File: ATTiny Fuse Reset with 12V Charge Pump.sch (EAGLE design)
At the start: 37 parts, among them IC1 ATTinyx5/13, IC2 ATTinyx4, U2 ARDUINOR3-BPLACE

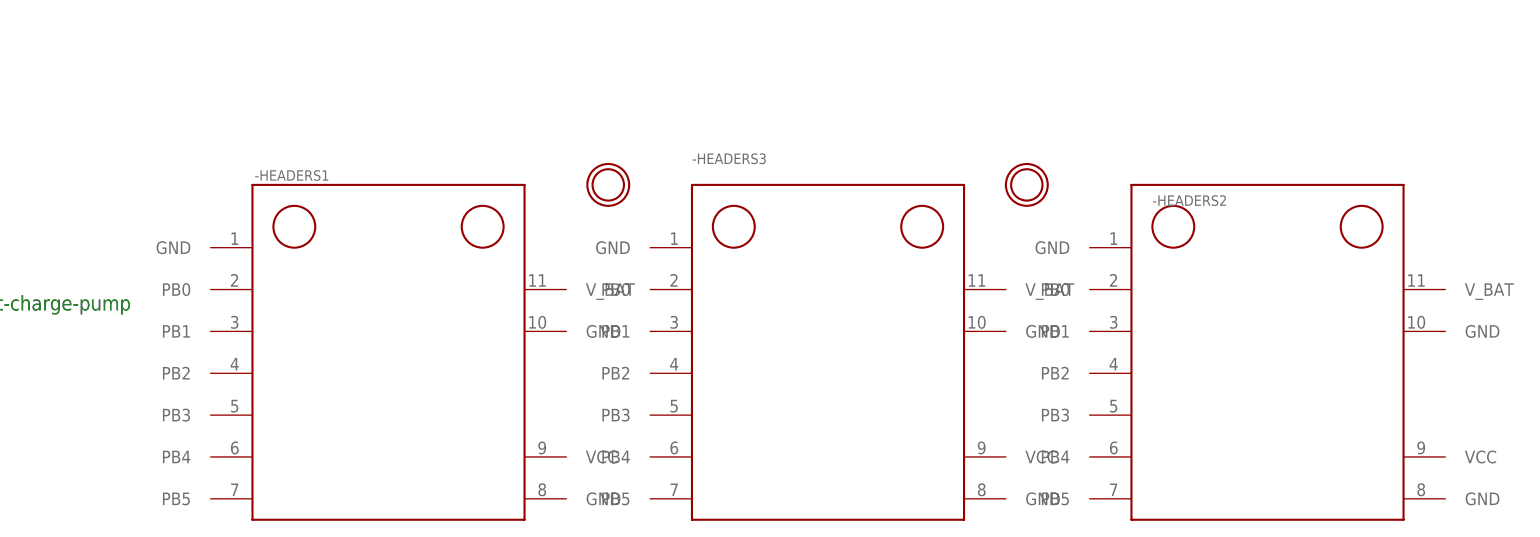
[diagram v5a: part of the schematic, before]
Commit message: changed attiny breakout size
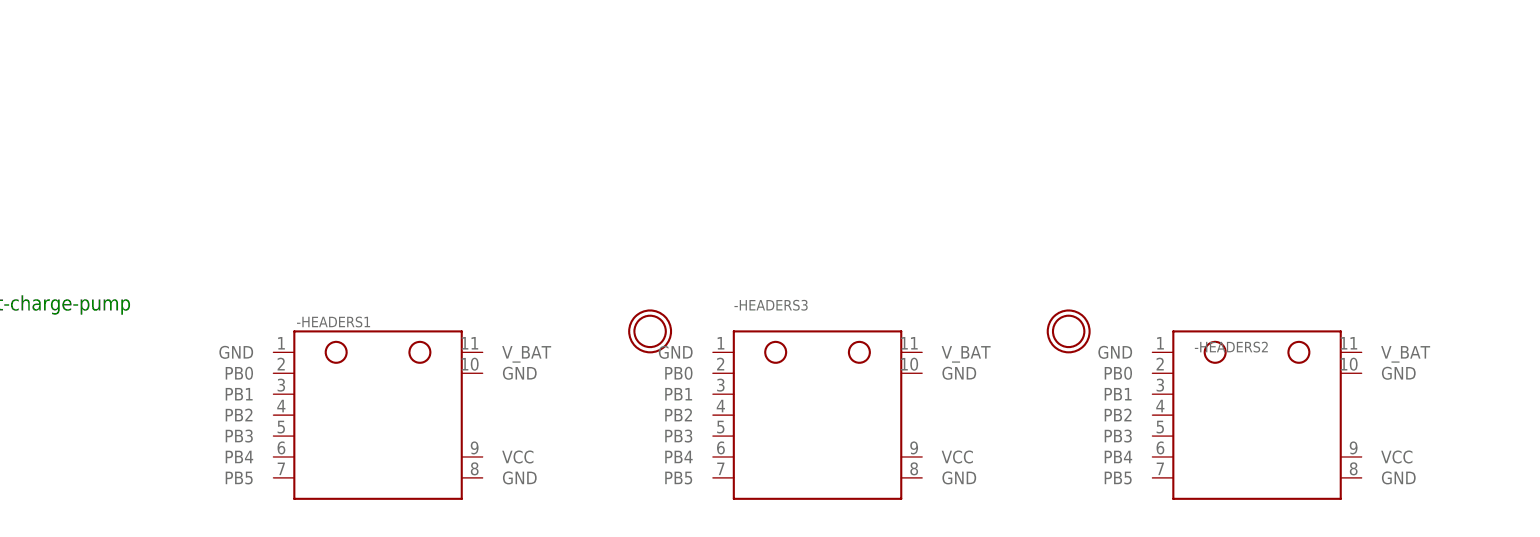
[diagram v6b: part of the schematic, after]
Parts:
- -HEADERS1, -HEADERS2: device ATtami:ATTANI_BREAKOUT_PINSNOHEAD -> ATtami:ATTANI_BREAKOUT_PINS
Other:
- moved on the sheet: -HEADERS1, -HEADERS2, -HEADERS3
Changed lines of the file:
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@@
 <grid distance="0.1" unitdist="inch" unit="inch" style="lines" multiple="1" display="no" altdistance="0.01" altunitdist="inch" altunit="inch"/>
 <layers>
-<layer number="1" name="Top" color="4" fill="1" visible="yes" active="no"/>
-<layer number="16" name="Bottom" color="1" fill="1" visible="yes" active="no"/>
-<layer number="17" name="Pads" color="2" fill="1" visible="yes" active="no"/>
-<layer number="18" name="Vias" color="2" fill="1" visible="yes" active="no"/>
-<layer number="19" name="Unrouted" color="6" fill="1" visible="yes" active="no"/>
-<layer number="20" name="Dimension" color="15" fill="1" visible="yes" active="no"/>
-<layer number="21" name="tPlace" color="7" fill="1" visible="yes" active="no"/>
-<layer number="22" name="bPlace" color="7" fill="1" visible="yes" active="no"/>
-<layer number="23" name="tOrigins" color="15" fill="1" visible="yes" active="no"/>
-<layer number="24" name="bOrigins" color="15" fill="1" visible="yes" active="no"/>
-<layer number="25" name="tNames" color="7" fill="1" visible="yes" active="no"/>
-<layer number="26" name="bNames" color="7" fill="1" visible="yes" active="no"/>
-<layer number="27" name="tValues" color="7" fill="1" visible="yes" active="no"/>
-<layer number="28" name="bValues" color="7" fill="1" visible="yes" active="no"/>
+<layer number="1" name="Top" color="4" fill="1" visible="no" active="no"/>
+<layer number="16" name="Bottom" color="1" fill="1" visible="no" active="no"/>
+<layer number="17" name="Pads" color="2" fill="1" visible="no" active="no"/>
+<layer number="18" name="Vias" color="2" fill="1" visible="no" active="no"/>
+<layer number="19" name="Unrouted" color="6" fill="1" visible="no" active="no"/>
+<layer number="20" name="Dimension" color="15" fill="1" visible="no" active="no"/>
+<layer number="21" name="tPlace" color="7" fill="1" visible="no" active="no"/>
+<layer number="22" name="bPlace" color="7" fill="1" visible="no" active="no"/>
+<layer number="23" name="tOrigins" color="15" fill="1" visible="no" active="no"/>
+<layer number="24" name="bOrigins" color="15" fill="1" visible="no" active="no"/>
+<layer number="25" name="tNames" color="7" fill="1" visible="no" active="no"/>
+<layer number="26" name="bNames" color="7" fill="1" visible="no" active="no"/>
+<layer number="27" name="tValues" color="7" fill="1" visible="no" active="no"/>
+<layer number="28" name="bValues" color="7" fill="1" visible="no" active="no"/>
 <layer number="29" name="tStop" color="7" fill="3" visible="no" active="no"/>
 <layer number="30" name="bStop" color="7" fill="6" visible="no" active="no"/>
@@
 <layer number="35" name="tGlue" color="7" fill="4" visible="no" active="no"/>
 <layer number="36" name="bGlue" color="7" fill="5" visible="no" active="no"/>
-<layer number="37" name="tTest" color="7" fill="1" visible="yes" active="no"/>
-<layer number="38" name="bTest" color="7" fill="1" visible="yes" active="no"/>
+<layer number="37" name="tTest" color="7" fill="1" visible="no" active="no"/>
+<layer number="38" name="bTest" color="7" fill="1" visible="no" active="no"/>
 <layer number="39" name="tKeepout" color="4" fill="11" visible="no" active="no"/>
 <layer number="40" name="bKeepout" color="1" fill="11" visible="no" active="no"/>
@@
 <layer number="44" name="Drills" color="7" fill="1" visible="no" active="no"/>
 <layer number="45" name="Holes" color="7" fill="1" visible="no" active="no"/>
-<layer number="46" name="Milling" color="3" fill="1" visible="yes" active="no"/>
-<layer number="47" name="Measures" color="7" fill="1" visible="yes" active="no"/>
-<layer number="48" name="Document" color="7" fill="1" visible="yes" active="no"/>
-<layer number="49" name="Reference" color="7" fill="1" visible="yes" active="no"/>
-<layer number="50" name="dxf" color="7" fill="1" visible="yes" active="no"/>
-<layer number="51" name="tDocu" color="7" fill="1" visible="yes" active="no"/>
-<layer number="52" name="bDocu" color="7" fill="1" visible="yes" active="no"/>
-<layer number="53" name="tGND_GNDA" color="7" fill="9" visible="yes" active="no"/>
-<layer number="54" name="bGND_GNDA" color="1" fill="9" visible="yes" active="no"/>
-<layer number="56" name="wert" color="7" fill="1" visible="yes" active="no"/>
-<layer number="57" name="tCAD" color="7" fill="1" visible="yes" active="no"/>
+<layer number="46" name="Milling" color="3" fill="1" visible="no" active="no"/>
+<layer number="47" name="Measures" color="7" fill="1" visible="no" active="no"/>
+<layer number="48" name="Document" color="7" fill="1" visible="no" active="no"/>
+<layer number="49" name="Reference" color="7" fill="1" visible="no" active="no"/>
+<layer number="50" name="dxf" color="7" fill="1" visible="no" active="no"/>
+<layer number="51" name="tDocu" color="7" fill="1" visible="no" active="no"/>
+<layer number="52" name="bDocu" color="7" fill="1" visible="no" active="no"/>
+<layer number="53" name="tGND_GNDA" color="7" fill="9" visible="no" active="no"/>
+<layer number="54" name="bGND_GNDA" color="1" fill="9" visible="no" active="no"/>
+<layer number="56" name="wert" color="7" fill="1" visible="no" active="no"/>
+<layer number="57" name="tCAD" color="7" fill="1" visible="no" active="no"/>
 <layer number="90" name="Modules" color="5" fill="1" visible="yes" active="yes"/>
 <layer number="91" name="Nets" color="2" fill="1" visible="yes" active="yes"/>
@@
 <part name="P+3" library="microbuilder" deviceset="VCC" device=""/>
 <part name="SUPPLY11" library="supply2" deviceset="GND" device=""/>
-<part name="-HEADERS1" library="ATtami" deviceset="ATTANI_BREAKOUT_PINS" device="NOHEAD" value="ATTami"/>
-<part name="-HEADERS2" library="ATtami" deviceset="ATTANI_BREAKOUT_PINS" device="NOHEAD"/>
+<part name="-HEADERS1" library="ATtami" deviceset="ATTANI_BREAKOUT_PINS" device="" value="ATTami"/>
+<part name="-HEADERS2" library="ATtami" deviceset="ATTANI_BREAKOUT_PINS" device=""/>
 <part name="-HEADERS3" library="ATtami" deviceset="ATTANI_BREAKOUT_PINS" device=""/>
 <part name="R11" library="ATtami" deviceset="RESISTOR" device="0805-RES" value="10K"/>
@@
 <attribute name="VALUE" x="-101.473" y="109.855" size="1.778" layer="96"/>
 </instance>
-<instance part="U$5" gate="G$1" x="-160.02" y="43.18"/>
-<instance part="U$6" gate="G$1" x="-109.22" y="43.18"/>
+<instance part="U$5" gate="G$1" x="-154.94" y="25.4"/>
+<instance part="U$6" gate="G$1" x="-104.14" y="25.4"/>
 <instance part="R9" gate="G$1" x="-66.04" y="109.22" smashed="yes" rot="R270">
 <attribute name="NAME" x="-63.7794" y="111.252" size="1.778" layer="95"/>
@@
 <attribute name="VALUE" x="-305.943" y="98.171" size="1.778" layer="96"/>
 </instance>
-<instance part="-HEADERS1" gate="G$1" x="-203.2" y="43.18" smashed="yes">
-<attribute name="NAME" x="-202.946" y="43.688" size="1.27" layer="95"/>
-</instance>
-<instance part="-HEADERS2" gate="G$1" x="-96.52" y="43.18" smashed="yes">
-<attribute name="NAME" x="-93.98" y="40.64" size="1.27" layer="95"/>
-</instance>
-<instance part="-HEADERS3" gate="G$1" x="-149.86" y="43.18" smashed="yes">
-<attribute name="NAME" x="-149.86" y="45.72" size="1.27" layer="95"/>
+<instance part="-HEADERS1" gate="G$1" x="-198.12" y="25.4" smashed="yes">
+<attribute name="NAME" x="-197.866" y="25.908" size="1.27" layer="95"/>
+</instance>
+<instance part="-HEADERS2" gate="G$1" x="-91.44" y="25.4" smashed="yes">
+<attribute name="NAME" x="-88.9" y="22.86" size="1.27" layer="95"/>
+</instance>
+<instance part="-HEADERS3" gate="G$1" x="-144.78" y="25.4" smashed="yes">
+<attribute name="NAME" x="-144.78" y="27.94" size="1.27" layer="95"/>
 </instance>
 <instance part="R11" gate="G$1" x="-200.66" y="111.76" smashed="yes" rot="R270">

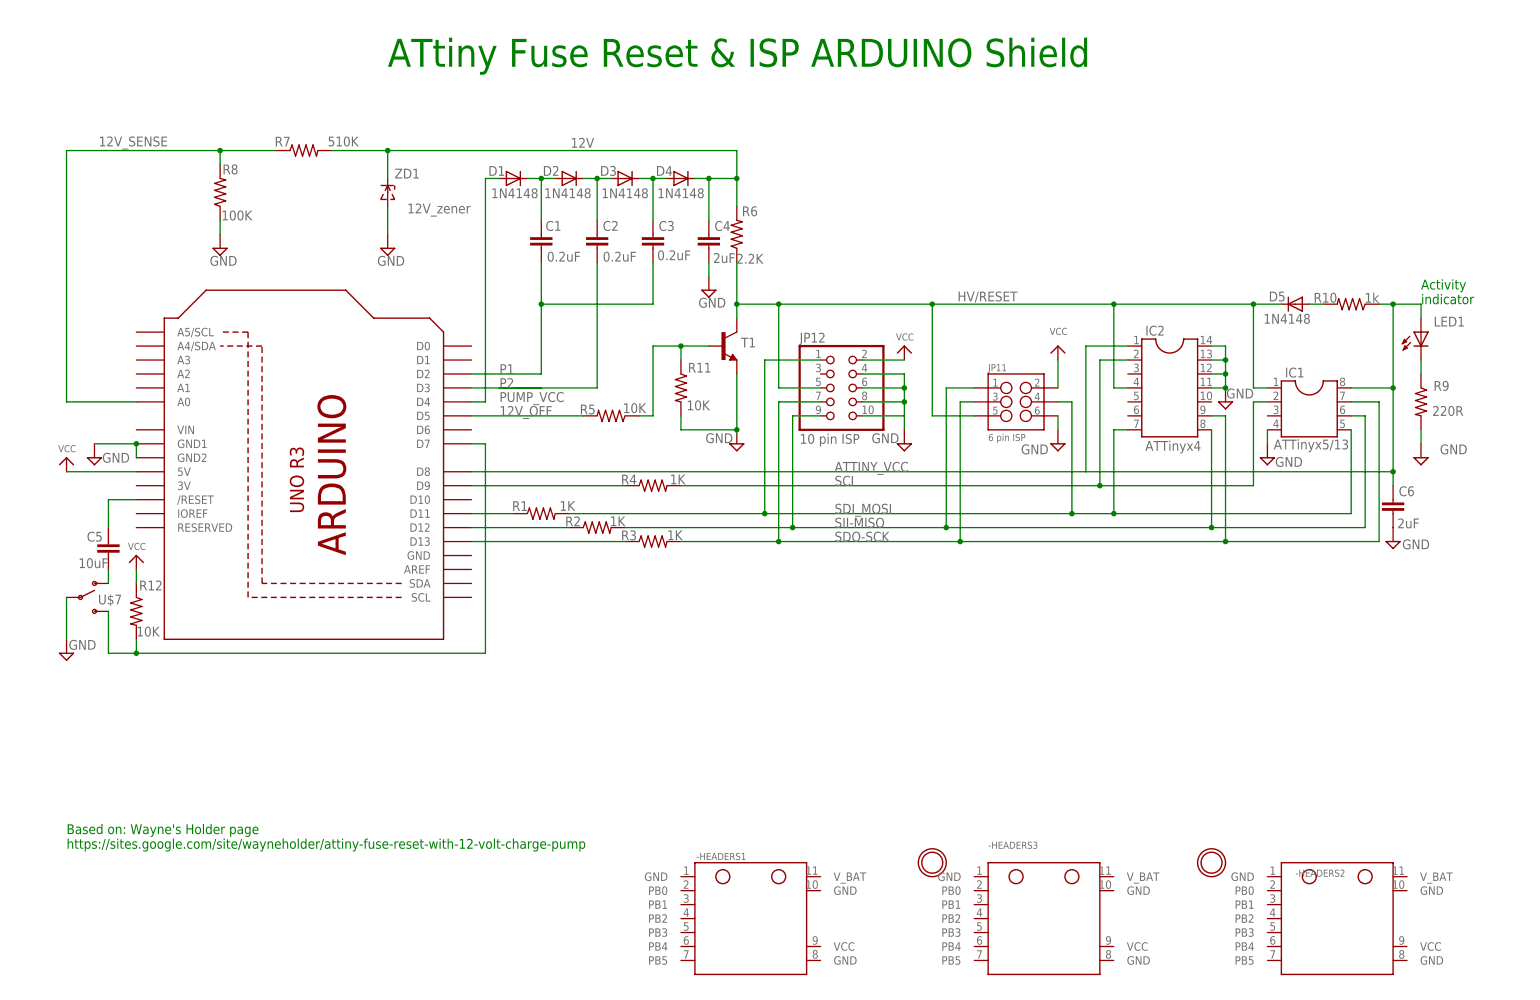
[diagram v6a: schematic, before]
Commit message: ATTami components connected
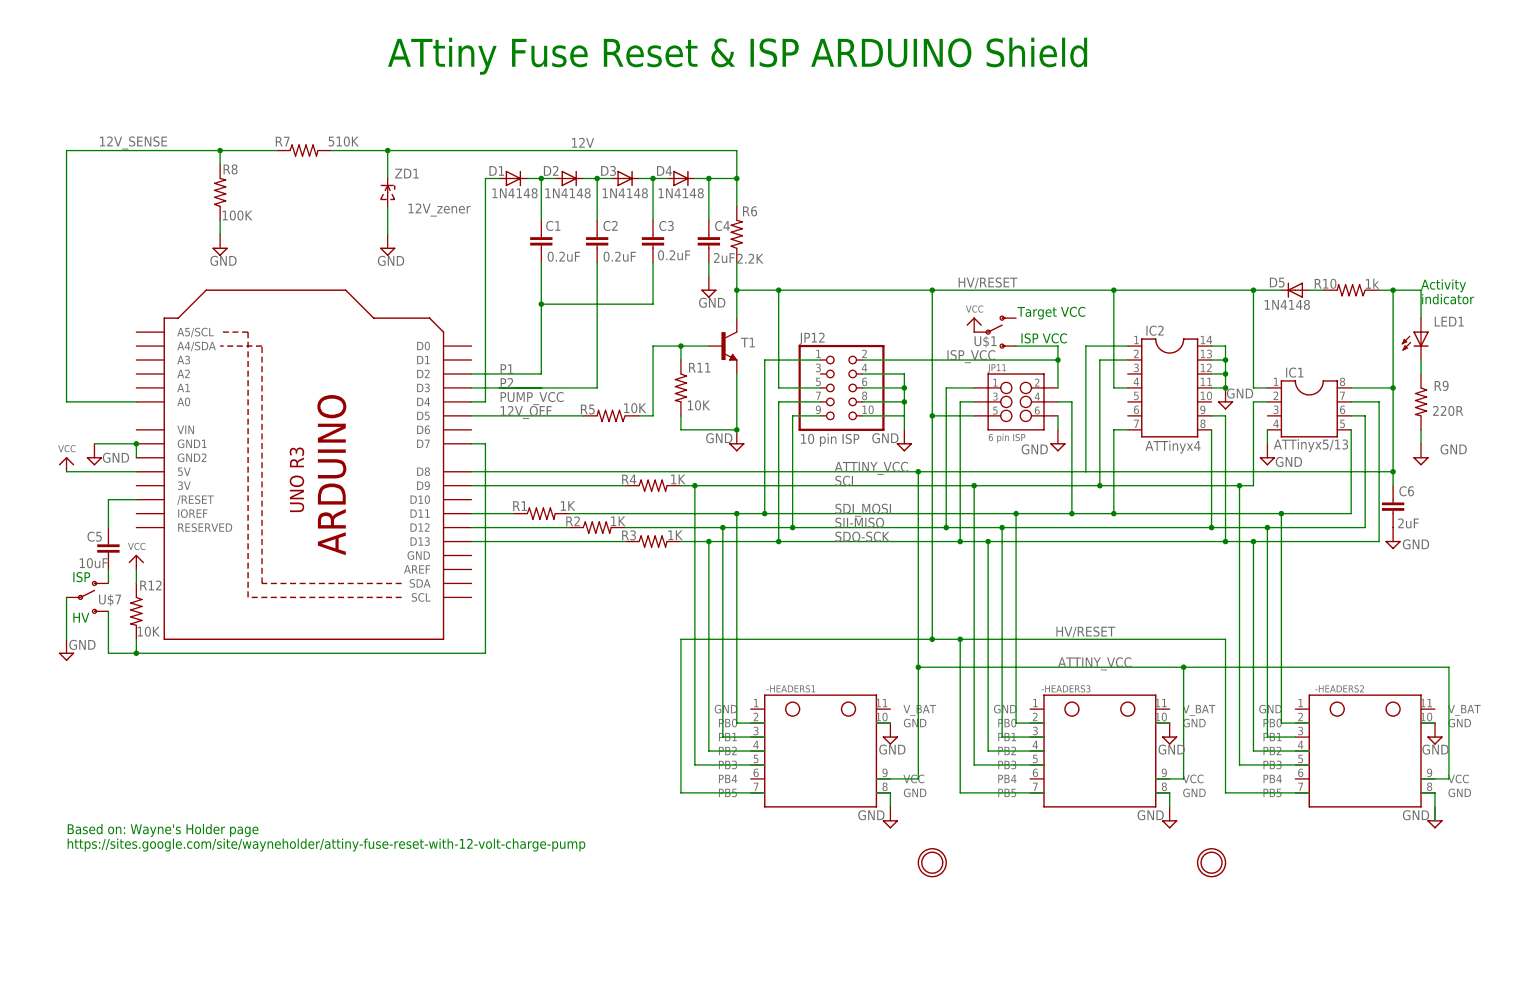
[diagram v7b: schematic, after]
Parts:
- added U$1: SWITCH_SPDT, SparkFun-Electromechanical:SWITCH_SPDT
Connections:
- new net ISP_VCC: JP11.2, JP12.2, U$1.S
- new net N$13: -HEADERS2.GND@2
- net ATTINY_VCC: now also -HEADERS1.VCC, -HEADERS2.VCC, -HEADERS3.VCC
- net GND: now also -HEADERS1.GND@1, -HEADERS1.GND@2, -HEADERS2.GND@1, -HEADERS3.GND@1, -HEADERS3.GND@2
- net HV/RESET: now also -HEADERS1.PB5, -HEADERS2.PB5, -HEADERS3.PB5
- net SCI: now also -HEADERS1.PB3, -HEADERS2.PB3, -HEADERS3.PB3
- net SDI_MOSI: now also -HEADERS1.PB0, -HEADERS2.PB0, -HEADERS3.PB0
- net SDO-SCK: now also -HEADERS1.PB2, -HEADERS2.PB2, -HEADERS3.PB2
- net SII-MISO: now also -HEADERS1.PB1, -HEADERS3.PB1
- net VCC: now also U$1.P; no longer JP11.2, JP12.2
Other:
- note added: "HV"
- note added: "ISP"
- note added: "ISP VCC"
- note added: "Target VCC"
- moved on the sheet: -HEADERS1, -HEADERS2, -HEADERS3, D5, R10

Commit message: Added 3 LEDs. The LEDs indicate activity and error
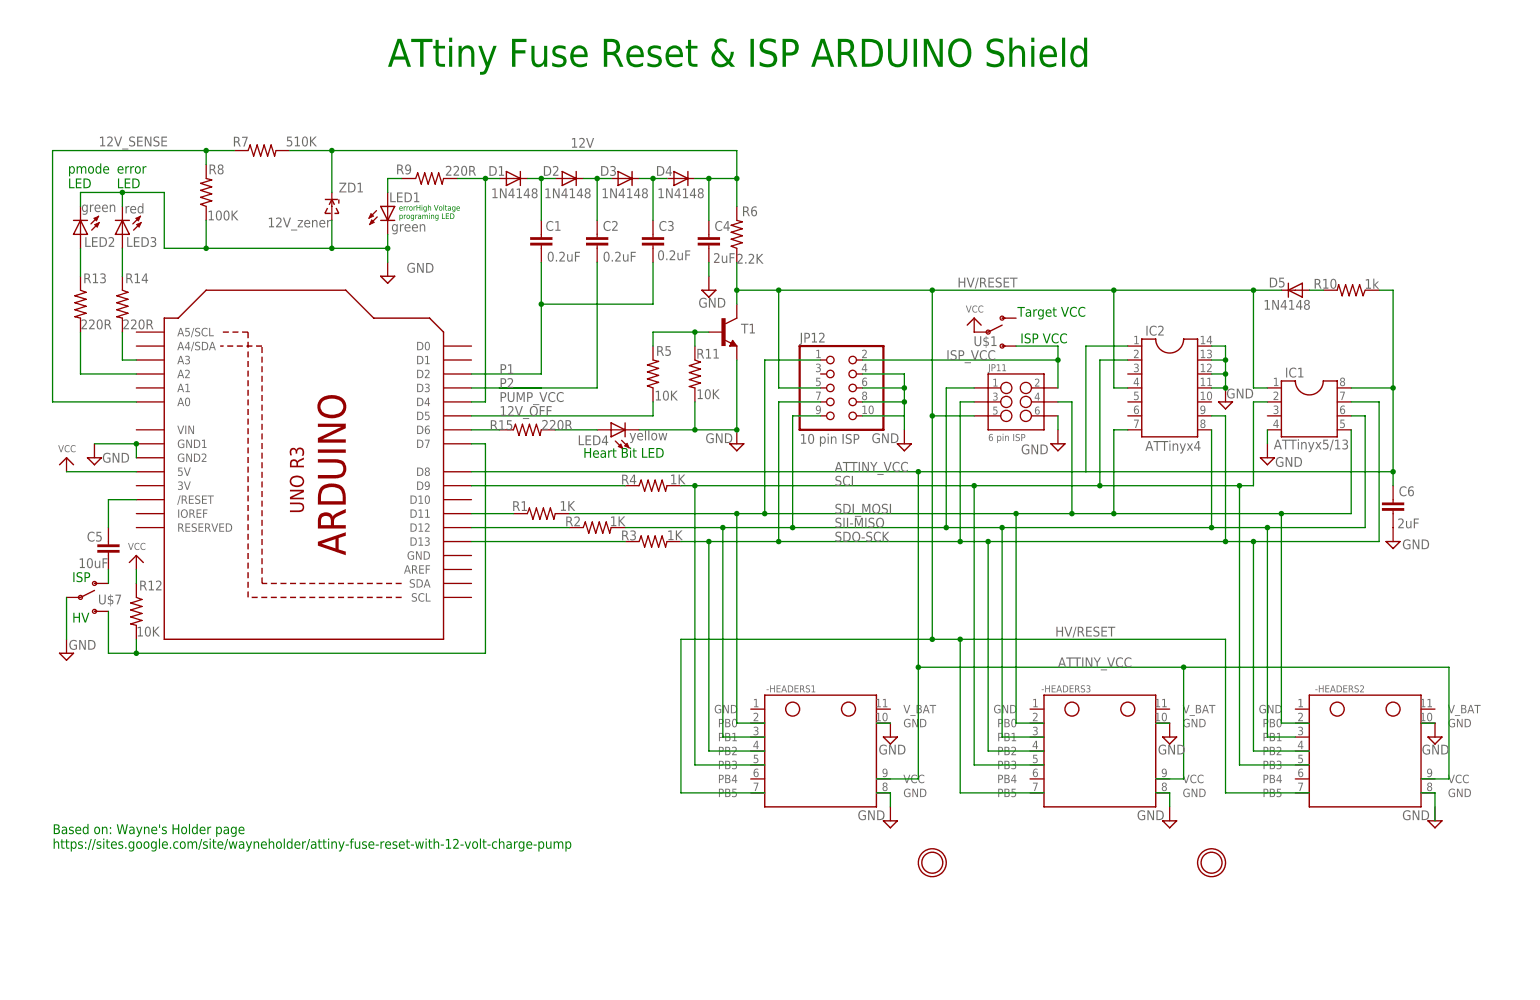
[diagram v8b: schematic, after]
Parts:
- added LED2: green, ATtami:LED-0805
- added LED3: red, ATtami:LED-0805
- added LED4: yellow, ATtami:LED-0805
- added R13, R14, R15: 220R, ATtami:RESISTOR0805-RES
- LED1: value (none) -> green
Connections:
- new net N$14: LED2.A, R13.1
- new net N$15: LED3.A, R14.1
- new net N$17: R14.2, U2.A3
- new net N$18: R13.2, U2.A2
- new net N$19: R15.1, U2.D6
- new net N$20: LED4.A, R15.2
- net 12V_OFF: now also R5.1; no longer R5.2
- net ATTINY_VCC: no longer LED1.A
- net GND: now also LED1.C, LED2.C, LED3.C, LED4.C; no longer R9.2
- net N$1: now also R5.2; no longer R5.1
- net N$4: now also LED1.A; no longer LED1.C
- net PUMP_VCC: now also R9.2
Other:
- note added: "Heart Bit LED"
- note added: "error LED"
- note added: "errorHigh Voltage programing LED"
- note added: "pmode LED"
- note removed: "Activity indicator"
- moved on the sheet: LED1, R11, R5, R7, R8, R9, T1, ZD1
